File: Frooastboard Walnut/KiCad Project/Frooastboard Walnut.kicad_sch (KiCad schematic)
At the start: 231 parts, among them SW1 SW_Push, U1 ATmega32U4-A, U2 IS31FL3737, Y1 Crystal_GND24_Small

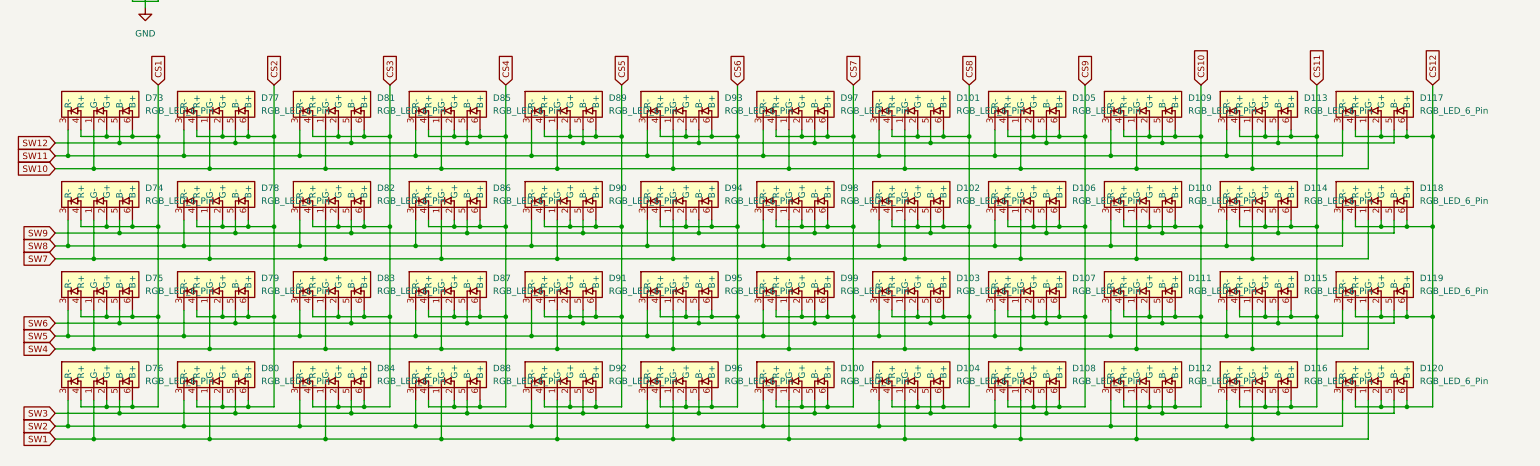
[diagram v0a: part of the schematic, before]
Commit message: switch leds
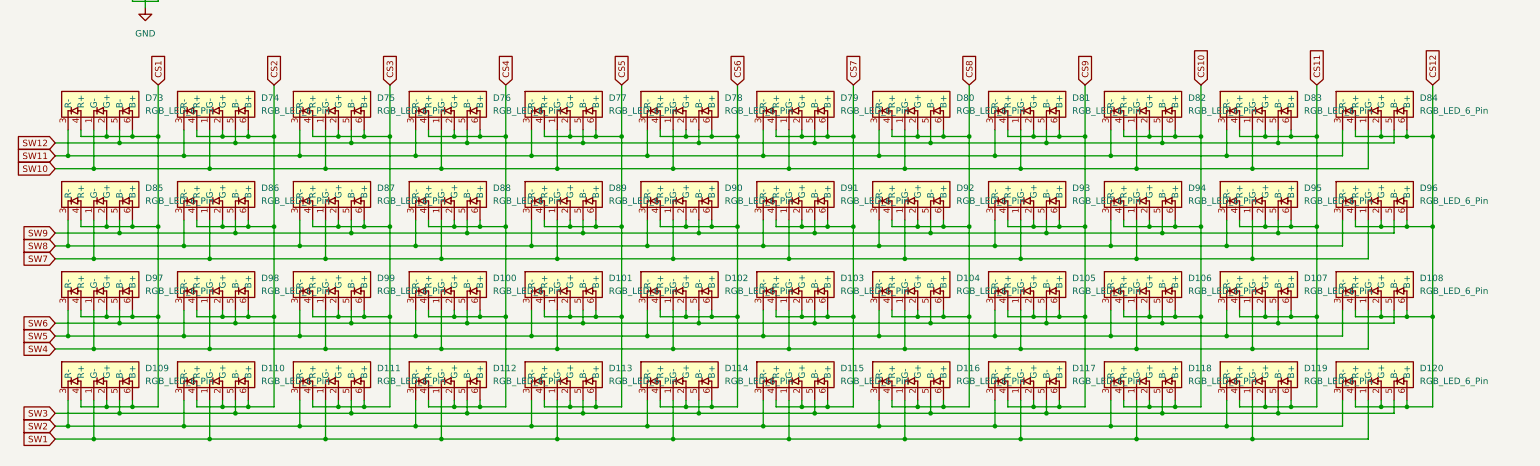
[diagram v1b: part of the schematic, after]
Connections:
- net CS1: now also D109.2 (G+), D109.4 (R+), D109.6 (B+), D85.2 (G+), D85.4 (R+), D85.6 (B+), D97.2 (G+), D97.4 (R+), D97.6 (B+); no longer D74.2 (G+), D74.4 (R+), D74.6 (B+), D75.2 (G+), D75.4 (R+), D75.6 (B+), D76.2 (G+), D76.4 (R+), D76.6 (B+)
- net CS10: now also D106.2 (G+), D106.4 (R+), D106.6 (B+), D118.2 (G+), D118.4 (R+), D118.6 (B+), D82.2 (G+), D82.4 (R+), D82.6 (B+), D94.2 (G+), D94.4 (R+), D94.6 (B+); no longer D109.2 (G+), D109.4 (R+), D109.6 (B+), D110.2 (G+), D110.4 (R+), D110.6 (B+), D111.2 (G+), D111.4 (R+), D111.6 (B+), D112.2 (G+), D112.4 (R+), D112.6 (B+)
- net CS11: now also D107.2 (G+), D107.4 (R+), D107.6 (B+), D119.2 (G+), D119.4 (R+), D119.6 (B+), D83.2 (G+), D83.4 (R+), D83.6 (B+), D95.2 (G+), D95.4 (R+), D95.6 (B+); no longer D113.2 (G+), D113.4 (R+), D113.6 (B+), D114.2 (G+), D114.4 (R+), D114.6 (B+), D115.2 (G+), D115.4 (R+), D115.6 (B+), D116.2 (G+), D116.4 (R+), D116.6 (B+)
- net CS12: now also D108.2 (G+), D108.4 (R+), D108.6 (B+), D84.2 (G+), D84.4 (R+), D84.6 (B+), D96.2 (G+), D96.4 (R+), D96.6 (B+); no longer D117.2 (G+), D117.4 (R+), D117.6 (B+), D118.2 (G+), D118.4 (R+), D118.6 (B+), D119.2 (G+), D119.4 (R+), D119.6 (B+)
- net CS2: now also D110.2 (G+), D110.4 (R+), D110.6 (B+), D74.2 (G+), D74.4 (R+), D74.6 (B+), D86.2 (G+), D86.4 (R+), D86.6 (B+), D98.2 (G+), D98.4 (R+), D98.6 (B+); no longer D77.2 (G+), D77.4 (R+), D77.6 (B+), D78.2 (G+), D78.4 (R+), D78.6 (B+), D79.2 (G+), D79.4 (R+), D79.6 (B+), D80.2 (G+), D80.4 (R+), D80.6 (B+)
- net CS3: now also D111.2 (G+), D111.4 (R+), D111.6 (B+), D75.2 (G+), D75.4 (R+), D75.6 (B+), D87.2 (G+), D87.4 (R+), D87.6 (B+), D99.2 (G+), D99.4 (R+), D99.6 (B+); no longer D81.2 (G+), D81.4 (R+), D81.6 (B+), D82.2 (G+), D82.4 (R+), D82.6 (B+), D83.2 (G+), D83.4 (R+), D83.6 (B+), D84.2 (G+), D84.4 (R+), D84.6 (B+)
- net CS4: now also D100.2 (G+), D100.4 (R+), D100.6 (B+), D112.2 (G+), D112.4 (R+), D112.6 (B+), D76.2 (G+), D76.4 (R+), D76.6 (B+); no longer D85.2 (G+), D85.4 (R+), D85.6 (B+), D86.2 (G+), D86.4 (R+), D86.6 (B+), D87.2 (G+), D87.4 (R+), D87.6 (B+)
- net CS5: now also D101.2 (G+), D101.4 (R+), D101.6 (B+), D113.2 (G+), D113.4 (R+), D113.6 (B+), D77.2 (G+), D77.4 (R+), D77.6 (B+); no longer D90.2 (G+), D90.4 (R+), D90.6 (B+), D91.2 (G+), D91.4 (R+), D91.6 (B+), D92.2 (G+), D92.4 (R+), D92.6 (B+)
- net CS6: now also D102.2 (G+), D102.4 (R+), D102.6 (B+), D114.2 (G+), D114.4 (R+), D114.6 (B+), D78.2 (G+), D78.4 (R+), D78.6 (B+), D90.2 (G+), D90.4 (R+), D90.6 (B+); no longer D93.2 (G+), D93.4 (R+), D93.6 (B+), D94.2 (G+), D94.4 (R+), D94.6 (B+), D95.2 (G+), D95.4 (R+), D95.6 (B+), D96.2 (G+), D96.4 (R+), D96.6 (B+)
- net CS7: now also D103.2 (G+), D103.4 (R+), D103.6 (B+), D115.2 (G+), D115.4 (R+), D115.6 (B+), D79.2 (G+), D79.4 (R+), D79.6 (B+), D91.2 (G+), D91.4 (R+), D91.6 (B+); no longer D100.2 (G+), D100.4 (R+), D100.6 (B+), D97.2 (G+), D97.4 (R+), D97.6 (B+), D98.2 (G+), D98.4 (R+), D98.6 (B+), D99.2 (G+), D99.4 (R+), D99.6 (B+)
- net CS8: now also D116.2 (G+), D116.4 (R+), D116.6 (B+), D80.2 (G+), D80.4 (R+), D80.6 (B+), D92.2 (G+), D92.4 (R+), D92.6 (B+); no longer D101.2 (G+), D101.4 (R+), D101.6 (B+), D102.2 (G+), D102.4 (R+), D102.6 (B+), D103.2 (G+), D103.4 (R+), D103.6 (B+)
- net CS9: now also D117.2 (G+), D117.4 (R+), D117.6 (B+), D81.2 (G+), D81.4 (R+), D81.6 (B+), D93.2 (G+), D93.4 (R+), D93.6 (B+); no longer D106.2 (G+), D106.4 (R+), D106.6 (B+), D107.2 (G+), D107.4 (R+), D107.6 (B+), D108.2 (G+), D108.4 (R+), D108.6 (B+)
- net SW1: now also D109.1 (G-), D110.1 (G-), D111.1 (G-), D113.1 (G-), D114.1 (G-), D115.1 (G-), D117.1 (G-), D118.1 (G-), D119.1 (G-); no longer D100.1 (G-), D104.1 (G-), D108.1 (G-), D76.1 (G-), D80.1 (G-), D84.1 (G-), D88.1 (G-), D92.1 (G-), D96.1 (G-)
- net SW10: now also D74.1 (G-), D75.1 (G-), D76.1 (G-), D78.1 (G-), D79.1 (G-), D80.1 (G-), D82.1 (G-), D83.1 (G-), D84.1 (G-); no longer D101.1 (G-), D105.1 (G-), D109.1 (G-), D113.1 (G-), D117.1 (G-), D85.1 (G-), D89.1 (G-), D93.1 (G-), D97.1 (G-)
- net SW11: now also D74.3 (R-), D75.3 (R-), D76.3 (R-), D78.3 (R-), D79.3 (R-), D80.3 (R-), D82.3 (R-), D83.3 (R-), D84.3 (R-); no longer D101.3 (R-), D105.3 (R-), D109.3 (R-), D113.3 (R-), D117.3 (R-), D85.3 (R-), D89.3 (R-), D93.3 (R-), D97.3 (R-)
- net SW12: now also D74.5 (B-), D75.5 (B-), D76.5 (B-), D78.5 (B-), D79.5 (B-), D80.5 (B-), D82.5 (B-), D83.5 (B-), D84.5 (B-); no longer D101.5 (B-), D105.5 (B-), D109.5 (B-), D113.5 (B-), D117.5 (B-), D85.5 (B-), D89.5 (B-), D93.5 (B-), D97.5 (B-)
- net SW2: now also D109.3 (R-), D110.3 (R-), D111.3 (R-), D113.3 (R-), D114.3 (R-), D115.3 (R-), D117.3 (R-), D118.3 (R-), D119.3 (R-); no longer D100.3 (R-), D104.3 (R-), D108.3 (R-), D76.3 (R-), D80.3 (R-), D84.3 (R-), D88.3 (R-), D92.3 (R-), D96.3 (R-)
- net SW3: now also D109.5 (B-), D110.5 (B-), D111.5 (B-), D113.5 (B-), D114.5 (B-), D115.5 (B-), D117.5 (B-), D118.5 (B-), D119.5 (B-); no longer D100.5 (B-), D104.5 (B-), D108.5 (B-), D76.5 (B-), D80.5 (B-), D84.5 (B-), D88.5 (B-), D92.5 (B-), D96.5 (B-)
- net SW4: now also D100.1 (G-), D101.1 (G-), D102.1 (G-), D104.1 (G-), D105.1 (G-), D106.1 (G-), D108.1 (G-), D97.1 (G-), D98.1 (G-); no longer D111.1 (G-), D115.1 (G-), D119.1 (G-), D75.1 (G-), D79.1 (G-), D83.1 (G-), D87.1 (G-), D91.1 (G-), D95.1 (G-)
- net SW5: now also D100.3 (R-), D101.3 (R-), D102.3 (R-), D104.3 (R-), D105.3 (R-), D106.3 (R-), D108.3 (R-), D97.3 (R-), D98.3 (R-); no longer D111.3 (R-), D115.3 (R-), D119.3 (R-), D75.3 (R-), D79.3 (R-), D83.3 (R-), D87.3 (R-), D91.3 (R-), D95.3 (R-)
- net SW6: now also D100.5 (B-), D101.5 (B-), D102.5 (B-), D104.5 (B-), D105.5 (B-), D106.5 (B-), D108.5 (B-), D97.5 (B-), D98.5 (B-); no longer D111.5 (B-), D115.5 (B-), D119.5 (B-), D75.5 (B-), D79.5 (B-), D83.5 (B-), D87.5 (B-), D91.5 (B-), D95.5 (B-)
- net SW7: now also D85.1 (G-), D87.1 (G-), D88.1 (G-), D89.1 (G-), D91.1 (G-), D92.1 (G-), D93.1 (G-), D95.1 (G-), D96.1 (G-); no longer D102.1 (G-), D106.1 (G-), D110.1 (G-), D114.1 (G-), D118.1 (G-), D74.1 (G-), D78.1 (G-), D82.1 (G-), D98.1 (G-)
- net SW8: now also D85.3 (R-), D87.3 (R-), D88.3 (R-), D89.3 (R-), D91.3 (R-), D92.3 (R-), D93.3 (R-), D95.3 (R-), D96.3 (R-); no longer D102.3 (R-), D106.3 (R-), D110.3 (R-), D114.3 (R-), D118.3 (R-), D74.3 (R-), D78.3 (R-), D82.3 (R-), D98.3 (R-)
- net SW9: now also D85.5 (B-), D87.5 (B-), D88.5 (B-), D89.5 (B-), D91.5 (B-), D92.5 (B-), D93.5 (B-), D95.5 (B-), D96.5 (B-); no longer D102.5 (B-), D106.5 (B-), D110.5 (B-), D114.5 (B-), D118.5 (B-), D74.5 (B-), D78.5 (B-), D82.5 (B-), D98.5 (B-)
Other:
- moved on the sheet: D100, D101, D102, D103, D104, D105, D106, D107, D108, D109, D110, D111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

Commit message: spacing
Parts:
- added R7: 20k, Resistor_SMD:R_0805_2012Metric, symbol Device:R
- added R8, R9: 10k, Resistor_SMD:R_0805_2012Metric, symbol Device:R
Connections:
- net +5V: now also U2.32 (VIO), R9.2
- net GND: now also U2.11 (PGND), U2.29 (AGND), U2.4 (PGND), R7.2, R8.2
- net RSET: now reaches U2.30 (RSET)
- net RSET: now also R7.1
- net SDB: now reaches U2.38 (~{SDB})
- net SDB: now also R9.1
- net IICRST: now reaches U2.39 (IICRST)
- net IICRST: now also R8.1

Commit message: update
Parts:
- added R10, R11: 2k, Resistor_SMD:R_0805_2012Metric, symbol Device:R
- R8, R9: value 10k -> 100k
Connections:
- net +5V: now also R10.1, R11.1
- net SCL: now also R11.2
- net SDA: now also R10.2
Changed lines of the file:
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@@
     (stroke (width 0) (type default) (color 0 0 0 0))
   )
+  (wire (pts (xy 162.56 26.67) (xy 162.56 30.48))
+    (stroke (width 0) (type default) (color 0 0 0 0))
+  )
   (wire (pts (xy 78.74 200.66) (xy 78.74 215.9))
     (stroke (width 0) (type default) (color 0 0 0 0))
@@
     (stroke (width 0) (type default) (color 0 0 0 0))
   )
+  (wire (pts (xy 162.56 38.1) (xy 162.56 41.91))
+    (stroke (width 0) (type default) (color 0 0 0 0))
+  )
   (wire (pts (xy 228.6 143.51) (xy 251.46 143.51))
     (stroke (width 0) (type default) (color 0 0 0 0))
@@
     (stroke (width 0) (type default) (color 0 0 0 0))
   )
+  (wire (pts (xy 172.72 26.67) (xy 172.72 30.48))
+    (stroke (width 0) (type default) (color 0 0 0 0))
+  )
   (wire (pts (xy 76.2 175.26) (xy 76.2 173.99))
     (stroke (width 0) (type default) (color 0 0 0 0))
@@
     (stroke (width 0) (type default) (color 0 0 0 0))
   )
+  (wire (pts (xy 172.72 38.1) (xy 172.72 41.91))
+    (stroke (width 0) (type default) (color 0 0 0 0))
+  )
   (wire (pts (xy 238.76 176.53) (xy 261.62 176.53))
     (stroke (width 0) (type default) (color 0 0 0 0))
@@
     )
   )
+  (global_label "SCL" (shape input) (at 172.72 41.91 270) (fields_autoplaced)
+    (effects (font (size 1.27 1.27)) (justify right))
+    (property "Intersheet References" "${INTERSHEET_REFS}" (id 0) (at 172.6406 47.8307 90)
+      (effects (font (size 1.27 1.27)) (justify right) hide)
+    )
+  )
   (global_label "COL4" (shape input) (at 116.84 196.85 90) (fields_autoplaced)
     (effects (font (size 1.27 1.27)) (justify left))
@@
     )
   )
+  (global_label "SDA" (shape input) (at 162.56 41.91 270) (fields_autoplaced)
+    (effects (font (size 1.27 1.27)) (justify right))
+    (property "Intersheet References" "${INTERSHEET_REFS}" (id 0) (at 162.4806 47.8912 90)
+      (effects (font (size 1.27 1.27)) (justify right) hide)
+    )
+  )
   (global_label "CS6" (shape input) (at 55.88 40.64 0) (fields_autoplaced)
     (effects (font (size 1.27 1.27)) (justify left))
@@
     (in_bom yes) (on_board yes) (fields_autoplaced)
     (property "Reference" "R9" (id 0) (at 143.51 24.13 90))
-    (property "Value" "10k" (id 1) (at 143.51 26.67 90))
+    (property "Value" "100k" (id 1) (at 143.51 26.67 90))
     (property "Footprint" "Resistor_SMD:R_0805_2012Metric" (id 2) (at 143.51 32.258 90)
       (effects (font (size 1.27 1.27)) hide)
@@
     )
   )
+  (symbol (lib_id "power:+5V") (at 162.56 26.67 0) (unit 1)
+    (in_bom yes) (on_board yes) (fields_autoplaced)
+    (property "Reference" "#PWR0110" (id 0) (at 162.56 30.48 0)
+      (effects (font (size 1.27 1.27)) hide)
+    )
+    (property "Value" "+5V" (id 1) (at 162.56 21.59 0))
+    (property "Footprint" "" (id 2) (at 162.56 26.67 0)
+      (effects (font (size 1.27 1.27)) hide)
+    )
+    (property "Datasheet" "" (id 3) (at 162.56 26.67 0)
+      (effects (font (size 1.27 1.27)) hide)
+    )
+    (pin "1")
+  )
   (symbol (lib_id "power:GND") (at 336.55 247.65 0) (unit 1)
     (in_bom yes) (on_board yes)
@@
     (pin "2")
   )
+  (symbol (lib_id "Device:R") (at 172.72 34.29 0) (unit 1)
+    (in_bom yes) (on_board yes) (fields_autoplaced)
+    (property "Reference" "R11" (id 0) (at 175.26 33.0199 0)
+      (effects (font (size 1.27 1.27)) (justify left))
+    )
+    (property "Value" "2k" (id 1) (at 175.26 35.5599 0)
+      (effects (font (size 1.27 1.27)) (justify left))
+    )
+    (property "Footprint" "Resistor_SMD:R_0805_2012Metric" (id 2) (at 170.942 34.29 90)
+      (effects (font (size 1.27 1.27)) hide)
+    )
+    (property "Datasheet" "~" (id 3) (at 172.72 34.29 0)
+      (effects (font (size 1.27 1.27)) hide)
+    )
+    (pin "1")
+    (pin "2")
+  )
   (symbol (lib_id "Frooastboard Symbols:RGB_LED_6_Pin") (at 280.67 149.225 0) (unit 1)
     (in_bom yes) (on_board yes) (fields_autoplaced)
@@
     (pin "4")
   )
+  (symbol (lib_id "power:+5V") (at 172.72 26.67 0) (unit 1)
+    (in_bom yes) (on_board yes) (fields_autoplaced)
+    (property "Reference" "#PWR0111" (id 0) (at 172.72 30.48 0)
+      (effects (font (size 1.27 1.27)) hide)
+    )
+    (property "Value" "+5V" (id 1) (at 172.72 21.59 0))
+    (property "Footprint" "" (id 2) (at 172.72 26.67 0)
+      (effects (font (size 1.27 1.27)) hide)
+    )
+    (property "Datasheet" "" (id 3) (at 172.72 26.67 0)
+      (effects (font (size 1.27 1.27)) hide)
+    )
+    (pin "1")
+  )
   (symbol (lib_id "MX_Alps_Hybrid:MX-NoLED") (at 92.71 219.71 0) (unit 1)
     (in_bom yes) (on_board yes) (fields_autoplaced)
@@
       (effects (font (size 1.27 1.27)) (justify left))
     )
-    (property "Value" "10k" (id 1) (at 130.81 35.5599 0)
+    (property "Value" "100k" (id 1) (at 130.81 35.5599 0)
       (effects (font (size 1.27 1.27)) (justify left))
     )
@@
     (pin "2")
   )
+  (symbol (lib_id "Device:R") (at 162.56 34.29 0) (unit 1)
+    (in_bom yes) (on_board yes) (fields_autoplaced)
+    (property "Reference" "R10" (id 0) (at 165.1 33.0199 0)
+      (effects (font (size 1.27 1.27)) (justify left))
+    )
+    (property "Value" "2k" (id 1) (at 165.1 35.5599 0)
+      (effects (font (size 1.27 1.27)) (justify left))
+    )
+    (property "Footprint" "Resistor_SMD:R_0805_2012Metric" (id 2) (at 160.782 34.29 90)
+      (effects (font (size 1.27 1.27)) hide)
+    )
+    (property "Datasheet" "~" (id 3) (at 162.56 34.29 0)
+      (effects (font (size 1.27 1.27)) hide)
+    )
+    (pin "1")
+    (pin "2")
+  )
   (symbol (lib_id "MX_Alps_Hybrid:MX-NoLED") (at 140.97 270.51 0) (unit 1)
     (in_bom yes) (on_board yes) (fields_autoplaced)
@@
       (reference "#PWR0109") (unit 1) (value "+5V") (footprint "")
     )
+    (path "/2f74359e-d216-4bab-b548-5f3ab7abb7bc"
+      (reference "#PWR0110") (unit 1) (value "+5V") (footprint "")
+    )
+    (path "/6b7082a6-1fce-48b2-a923-2546535775f7"
+      (reference "#PWR0111") (unit 1) (value "+5V") (footprint "")
+    )
     (path "/ffece364-b5a6-404e-be9c-a6280ec0760c"
       (reference "C1") (unit 1) (value "1u") (footprint "Capacitor_SMD:C_0805_2012Metric")
@@
     )
     (path "/6f723bd4-40b0-400b-842e-4939b975375f"
-      (reference "R8") (unit 1) (value "10k") (footprint "Resistor_SMD:R_0805_2012Metric")
+      (reference "R8") (unit 1) (value "100k") (footprint "Resistor_SMD:R_0805_2012Metric")
     )
     (path "/1b996097-de89-496a-9557-2e5d836190cf"
-      (reference "R9") (unit 1) (value "10k") (footprint "Resistor_SMD:R_0805_2012Metric")
+      (reference "R9") (unit 1) (value "100k") (footprint "Resistor_SMD:R_0805_2012Metric")
+    )
+    (path "/ed87153c-3ea6-483e-a170-cb4947c4a666"
+      (reference "R10") (unit 1) (value "2k") (footprint "Resistor_SMD:R_0805_2012Metric")
+    )
+    (path "/40944361-6ff4-4ffa-8e13-fc59fc424577"
+      (reference "R11") (unit 1) (value "2k") (footprint "Resistor_SMD:R_0805_2012Metric")
     )
     (path "/1bd7adc2-4e00-4b33-ab72-db693188d8ad"
